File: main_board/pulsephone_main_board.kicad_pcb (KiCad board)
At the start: 4 copper layers, 70.5 x 128.5 mm, 90 parts, among them J1 USB_C_Receptacle_USB2.0_14P, J2 Conn_01x05, J3 Conn_2Rows-35Pins_MountingPin, J4 Conn_2Rows-35Pins_MountingPin, J5 Conn_2Rows-35Pins_MountingPin, J7 Micro_SD_Card_Det1, SW1 SW_Push, SW2 SW_Push, U1 XL1509-3.3, U2 PCM5102APWR, U4 TPS63020DSJR/3.7V Reg, U5 TP4056-42-ESOP8

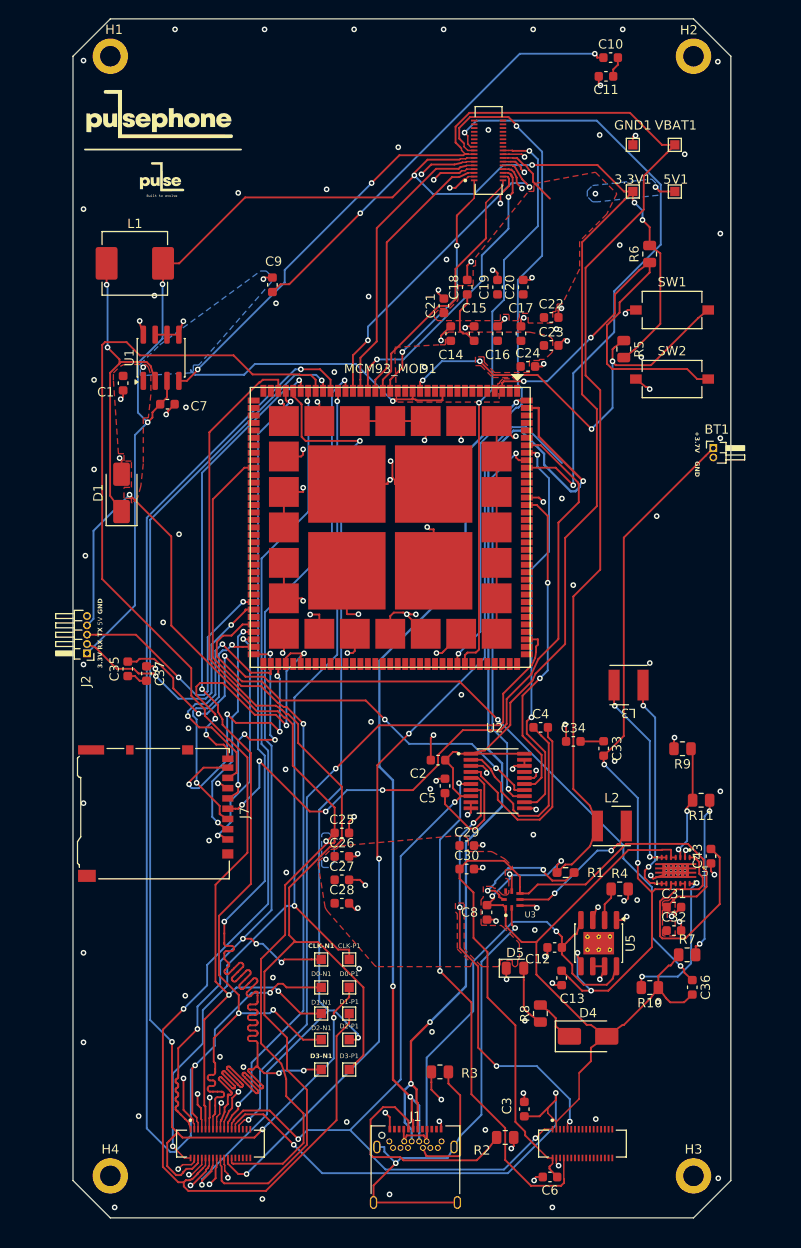
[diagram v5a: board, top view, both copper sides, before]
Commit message: footprint size adjustments for better part compatibility when ordering
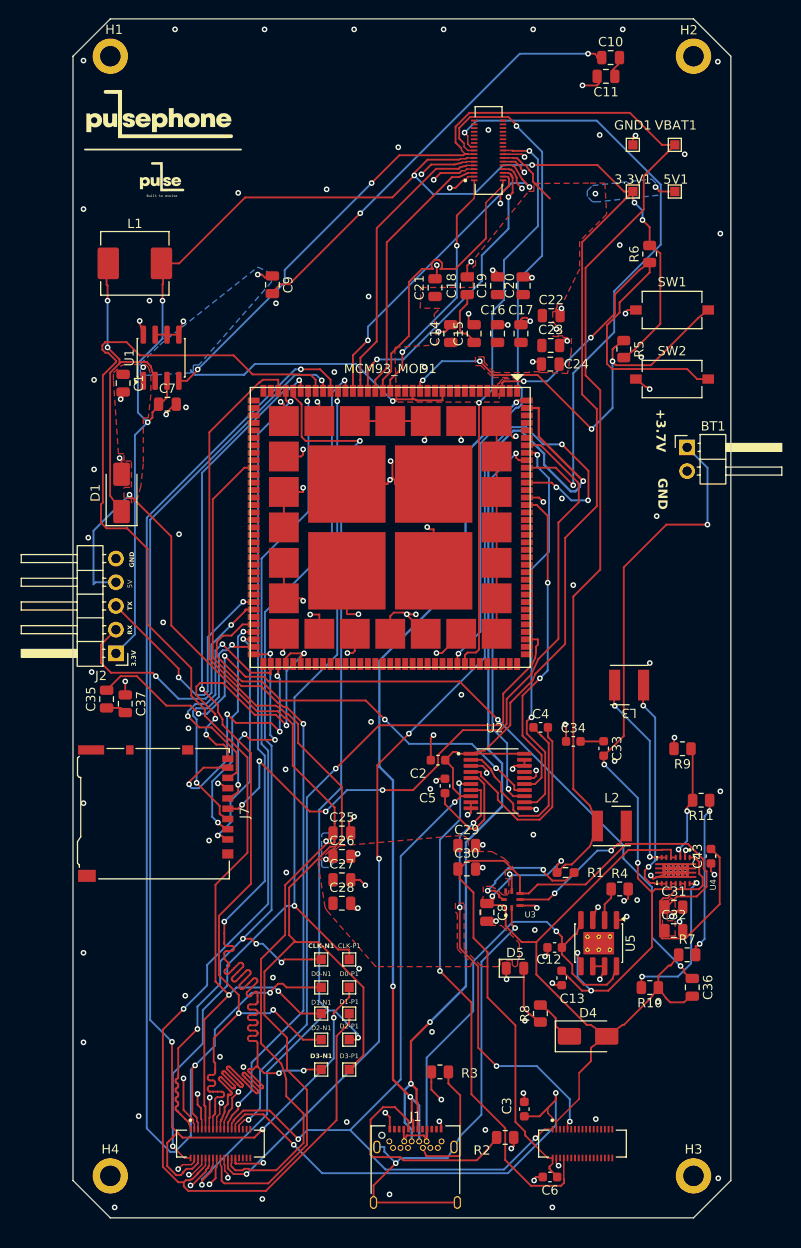
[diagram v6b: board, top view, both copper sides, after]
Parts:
- BT1: footprint Connector_PinHeader_1.00mm:PinHeader_1x02_P1.00mm_Horizontal -> Connector_PinHeader_2.54mm:PinHeader_1x02_P2.54mm_Horizontal
- C1, C10, C11, C14, C15, C16, C17, C18, C19, C20, C21, C22, C23, C24, C25, C26, C27, C28, C29, C30, C31, C32, C35, C36, C37, C7, C8, C9: footprint Capacitor_SMD:C_0603_1608Metric -> Capacitor_SMD:C_0805_2012Metric
- J2: footprint Connector_PinHeader_1.00mm:PinHeader_1x05_P1.00mm_Horizontal -> Connector_PinHeader_2.54mm:PinHeader_1x05_P2.54mm_Horizontal
- L1: value 47uh/2A -> 47uh; footprint Inductor_SMD:L_APV_APH0630 -> Inductor_SMD:L_KOHERelec_MDA7030
- R9: value 180 kΩ -> 174 kΩ
- moved C35 3.96 mm to (104.6, 98.9)
- moved C37 3.96 mm to (106.6, 99.4)
- moved J2 3.10 mm to (105.6, 94.0)
- moved BT1 2.81 mm to (166.8, 71.9)
- moved C24 2.41 mm to (152.2, 63.0), turned to 180 degrees
- moved C21 2.17 mm to (139.8, 54.8)
- moved C22 0.20 mm to (152.2, 57.8)
- moved C18 0.15 mm to (143.2, 54.6)
- moved C19 0.15 mm to (146.5, 54.6)
- moved C20 0.15 mm to (149.2, 54.6)
- moved L3 0.06 mm to (160.6, 97.4)
- moved C23 0.05 mm to (152.2, 61.0)
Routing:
- net /I2C3_SDA: track 102.0 -> 116.0 mm, vias 3 -> 6
- net GND: track 251.1 -> 258.0 mm, vias 163 -> 162
- net /CSI_CLK_P: track 28.5 -> 32.0 mm
- net Net-(BT1-+): track 82.4 -> 85.7 mm, vias 4 -> 5
- net /DSI_D1_N: track 131.0 -> 133.8 mm
- net UART_RX: track 27.3 -> 29.2 mm
- net Net-(C35-Pad2): track 87.3 -> 88.7 mm
- net +3.3V: track 302.8 -> 301.5 mm
- net UART_TX: track 28.1 -> 26.8 mm
- net +5V: track 238.2 -> 237.6 mm

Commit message: final review change (board was ordered, prod ready verSion)
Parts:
- added AUD-L1: TestPoint, TestPoint:TestPoint_Pad_1.0x1.0mm, F.Cu at (164.2, 141.0)
- added AUD-R1: TestPoint, TestPoint:TestPoint_Pad_1.0x1.0mm, F.Cu at (164.1, 143.9)
- added I2C3-SCL1: TestPoint, TestPoint:TestPoint_Pad_D1.0mm, F.Cu at (128.4, 148.8)
- added I2C3-SDA1: TestPoint, TestPoint:TestPoint_Pad_D1.0mm, F.Cu at (128.4, 152.2)
- 3.3V1, 5V1, CLK-N1, CLK-P1, D0-N1, D0-P1, D1-N1, D1-P1, D2-N1, D2-P1, D3-N1, D3-P1, GND1, VBAT1: footprint TestPoint:TestPoint_Pad_1.0x1.0mm -> TestPoint:TestPoint_Pad_D1.0mm
- J1: footprint Connector_USB:USB_C_Receptacle_Amphenol_12401548E4-2A -> Connector_USB:USB_C_Receptacle_HRO_TYPE-C-31-M-12
- ON/OFF1: renamed from SW2; footprint Button_Switch_SMD:SW_Tactile_SPST_NO_Straight_CK_PTS636Sx25SMTRLFS -> SSSS810701:SSSS810701
- RESET1: renamed from SW1; footprint Button_Switch_SMD:SW_Tactile_SPST_NO_Straight_CK_PTS636Sx25SMTRLFS -> Button_Switch_SMD:SW_Push_1P1T-SH_NO_CK_KMR2xxG
- moved ON/OFF1 4.71 mm to (169.8, 63.6), turned to 90 degrees
- moved J1 1.80 mm to (137.7, 151.8)
- moved C10 0.52 mm to (158.1, 30.1)
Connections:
- J1 pad S1: GNDCHASSIS -> GND
- J7 pad 10: unconnected-(J7-SHIELD-Pad10) -> GND
- ON/OFF1 pad 2: ONOFF -> unconnected-(ON/OFF1-Pad2)
- U5 pad 9: unconnected-(U5-EPAD-Pad9) -> GND
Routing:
- net +5V: track 237.6 -> 357.5 mm, vias 8 -> 4
- net GNDCHASSIS: track 52.8 -> 0.00 mm, vias 2 -> 0
- net /DSI_D3_N: track 136.6 -> 96.8 mm
- net SD2_CD_B: track 34.8 -> 70.8 mm, vias 4 -> 2
- net /DSI_CLK_P: track 100.1 -> 133.1 mm
- net /DSI_D1_N: track 133.8 -> 103.9 mm, vias 2 -> 4
- net /DSI_D2_P: track 108.4 -> 128.4 mm
- net Net-(J5-Pin_9): track 45.9 -> 65.0 mm, vias 4 -> 2
- net /DSI_D0_P: track 130.8 -> 111.6 mm, vias 4 -> 3
- net USB_DN: track 110.2 -> 92.4 mm, vias 3 -> 4
- net /DSI_D0_N: track 133.2 -> 116.5 mm, vias 3 -> 4
- net /I2C3_SDA: track 116.0 -> 99.8 mm, vias 6 -> 3
- net Net-(J5-Pin_8): track 55.8 -> 71.6 mm
- net CAM_I2C_SCL: track 73.7 -> 89.3 mm
- net +3.3V: track 301.5 -> 286.7 mm, vias 9 -> 6
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- removed copper zone on B.Cu, net +5V
- removed copper zone on F.Cu, net +5V

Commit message: restart project for summer, misc changes
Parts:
- removed CLK-N1, CLK-P1, D0-N1, D0-P1, D1-N1, D1-P1, D2-N1, D2-P1, D3-N1, D3-P1: TestPoint, TestPoint:TestPoint_Pad_D1.0mm
- removed D1: D_Schottky, Diode_SMD:D_SMA
- removed L1: 47uh, Inductor_SMD:L_KOHERelec_MDA7030
- added J6: Conn_01x01_Socket, Connector_Coaxial:U.FL_Hirose_U.FL-R-SMT-1_Vertical, F.Cu at (103.0, 121.3)
- added U6: LBEE5KL1YN-814, footprints:XCVR_LBEE5KL1YN-814, F.Cu at (110.5, 121.3)
- added Y1: XO53, Oscillator:Oscillator_SMD_EuroQuartz_XO53-4Pin_5.0x3.2mm, F.Cu at (108.7, 130.3)
- 3.3V1, 5V1, GND1, I2C3-SCL1, I2C3-SDA1, VBAT1: footprint TestPoint:TestPoint_Pad_D1.0mm -> TestPoint:TestPoint_Pad_D2.5mm
- C1, C7: value 22uF -> 1uF; footprint Capacitor_SMD:C_0805_2012Metric -> Capacitor_SMD:C_0603_1608Metric
- U1: value XL1509-3.3 -> AP2112K-3.3; footprint Package_SO:SOIC-8_3.9x4.9mm_P1.27mm -> Package_TO_SOT_SMD:SOT-23-5
- moved C11 61.2 mm to (166.8, 92.7)
- moved C10 60.9 mm to (168.3, 90.2), turned to 180 degrees
- moved C9 59.7 mm to (158.3, 102.2), turned to 180 degrees
- moved U1 51.9 mm to (151.4, 94.1)
- moved C1 51.9 mm to (147.8, 96.2), turned to 90 degrees
- moved C7 44.5 mm to (147.1, 93.5)
- moved R5 40.2 mm to (169.0, 100.5), turned to 90 degrees
- moved C28 39.3 mm to (157.6, 93.0), turned to 90 degrees
- moved C35 37.3 mm to (138.8, 113.8), turned to 180 degrees
- moved C37 36.3 mm to (138.8, 116.3), turned to 0 degrees
- moved C26 33.0 mm to (155.1, 94.5), turned to 90 degrees
- moved C27 31.7 mm to (154.6, 98.5), turned to -90 degrees
- moved C31 31.2 mm to (160.1, 90.5), turned to 90 degrees
- moved C30 29.3 mm to (160.8, 93.7)
- moved C25 26.5 mm to (151.3, 97.7), turned to 180 degrees
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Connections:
- C1 pad 1: +5V -> GND
- C1 pad 2: GND -> +5V
- C7 pad 1: +3.3V -> GND
- C7 pad 2: GND -> +3.3V
- MCM93_MOD1 pad 100: unconnected-(MCM93_MOD1C-30-Pad100) -> BT_UART_RTS_N
- MCM93_MOD1 pad 101: unconnected-(MCM93_MOD1C-31-Pad101) -> BT_UART_CTS_N
- MCM93_MOD1 pad 102: unconnected-(MCM93_MOD1C-32-Pad102) -> BT_UART_R
- MCM93_MOD1 pad 103: unconnected-(MCM93_MOD1C-33-Pad103) -> BT_UART_T
- MCM93_MOD1 pad 104: unconnected-(MCM93_MOD1C-34-Pad104) -> REG_ON_WL
- MCM93_MOD1 pad 105: unconnected-(MCM93_MOD1C-35-Pad105) -> REG_ON_BL
- MCM93_MOD1 pad 109: unconnected-(MCM93_MOD1D-4-Pad109) -> SDIO_CLK
- MCM93_MOD1 pad 110: unconnected-(MCM93_MOD1D-5-Pad110) -> SDIO_2
- MCM93_MOD1 pad 111: unconnected-(MCM93_MOD1D-6-Pad111) -> SDIO_3
- MCM93_MOD1 pad 112: unconnected-(MCM93_MOD1D-7-Pad112) -> SDIO_1
- MCM93_MOD1 pad 113: unconnected-(MCM93_MOD1D-8-Pad113) -> SDIO_CMD
- MCM93_MOD1 pad 114: unconnected-(MCM93_MOD1D-9-Pad114) -> SDIO_0
- MCM93_MOD1 pad 51: unconnected-(MCM93_MOD1B-16-Pad51) -> PCM_OUT
- MCM93_MOD1 pad 54: unconnected-(MCM93_MOD1B-19-Pad54) -> PCM_SYNC
- MCM93_MOD1 pad 56: unconnected-(MCM93_MOD1B-21-Pad56) -> PCM_CLK
- MCM93_MOD1 pad 58: unconnected-(MCM93_MOD1B-23-Pad58) -> PCM_IN
- MCM93_MOD1 pad 85: unconnected-(MCM93_MOD1C-15-Pad85) -> GPIO_WF_2
- MCM93_MOD1 pad 93: unconnected-(MCM93_MOD1C-23-Pad93) -> GPIO_WF_1
- MCM93_MOD1 pad 94: unconnected-(MCM93_MOD1C-24-Pad94) -> GPIO_WF_0
- U1 pad 2: Net-(D1-K) -> GND
- U1 pad 3: +3.3V -> +5V
- U1 pad 4: +3.7VBAT -> unconnected-(U1-NC-Pad4)
- U1 pad 5: GND -> +3.3V
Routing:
- net +5V: track 357.5 -> 56.8 mm, vias 4 -> 44
- net GND: track 263.0 -> 159.2 mm, vias 177 -> 123
- net +3.7VBAT: track 291.7 -> 210.0 mm, vias 7 -> 10
- net SDIO_3: track 0.00 -> 76.6 mm, vias 0 -> 8
- net BT_UART_T: track 0.00 -> 69.3 mm
- net BT_UART_CTS_N: track 0.00 -> 68.8 mm, vias 0 -> 2
- net SDIO_1: track 0.00 -> 68.2 mm, vias 0 -> 8
- net BT_UART_RTS_N: track 0.00 -> 68.0 mm, vias 0 -> 2
- net BT_UART_R: track 0.00 -> 68.0 mm
- net PCM_SYNC: track 0.00 -> 66.3 mm
- net PCM_OUT: track 0.00 -> 65.4 mm, vias 0 -> 2
- net SDIO_0: track 0.00 -> 63.6 mm, vias 0 -> 6
- net SDIO_CLK: track 0.00 -> 63.0 mm, vias 0 -> 4
- net Net-(C35-Pad2): track 80.5 -> 18.6 mm, vias 4 -> 2
- net SDIO_2: track 0.00 -> 61.5 mm, vias 0 -> 8
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- added copper zone on In2.Cu, net +5V
- removed copper zone on In2.Cu, net GND
